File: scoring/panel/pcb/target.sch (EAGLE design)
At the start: 13 parts, among them J1 AVRISP6_COMPACT, U1 ATTINY85-20SU

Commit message: target panel: Get BOM into shape, and make an openoffice version with total and mechanical parts.
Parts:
- C1: PRICE10 (none) -> 0.05
- HIT: PRICE10 (none) -> 0.288
- J1: DPN (none) -> OR1108-ND; PRICE10 (none) -> 0.399
- JP1: DPN (none) -> 952-2245-ND; PRICE10 (none) -> 0.155
- JP2: DPN (none) -> 102-1170-ND; PRICE10 (none) -> 1.833
- PWR: PRICE10 (none) -> 0.267
- R1, R2, R3, R4: PRICE10 (none) -> 0.0196
- R6: DPN (none) -> P100ACT-ND; PRICE10 (none) -> 0.0196
- U1: PRICE10 (none) -> 1.386
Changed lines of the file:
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@@
 <part name="U1" library="Atmel_By_element14_Batch_1-00" deviceset="ATTINY85-20SU" device="">
 <attribute name="DPN" value="ATTINY85-20SU-ND"/>
+<attribute name="PRICE10" value="1.386"/>
 </part>
 <part name="P+1" library="supply1" deviceset="VCC" device=""/>
@@
 <part name="C1" library="rcl" deviceset="C-US" device="C0805" value=".1uF">
 <attribute name="DPN" value="399-1168-1-ND"/>
+<attribute name="PRICE10" value="0.05"/>
 </part>
 <part name="PWR" library="led" deviceset="LED" device="SML0805">
 <attribute name="DPN" value="160-1469-1-ND"/>
+<attribute name="PRICE10" value="0.267"/>
 </part>
 <part name="HIT" library="led" deviceset="LED" device="SML0805">
 <attribute name="DPN" value="160-1414-1-ND"/>
+<attribute name="PRICE10" value="0.288"/>
 </part>
 <part name="R1" library="rcl" deviceset="R-US_" device="R0805" value="680">
 <attribute name="DPN" value="P680ACT-ND"/>
+<attribute name="PRICE10" value="0.0196"/>
 </part>
 <part name="R2" library="rcl" deviceset="R-US_" device="R0805" value="680">
 <attribute name="DPN" value="P680ACT-ND"/>
+<attribute name="PRICE10" value="0.0196"/>
 </part>
 <part name="R3" library="rcl" deviceset="R-US_" device="R0805" value="10k">
 <attribute name="DPN" value="P10KACT-ND"/>
+<attribute name="PRICE10" value="0.0196"/>
 </part>
 <part name="R4" library="rcl" deviceset="R-US_" device="R0805" value="10k">
 <attribute name="DPN" value="P10KACT-ND"/>
+<attribute name="PRICE10" value="0.0196"/>
 </part>
 <part name="GND2" library="supply1" deviceset="GND" device=""/>
 <part name="P+2" library="supply1" deviceset="VCC" device=""/>
 <part name="P+3" library="supply1" deviceset="VCC" device=""/>
-<part name="J1" library="target" deviceset="AVRISP6" device="_COMPACT" value="AVRISP6_COMPACT"/>
+<part name="J1" library="target" deviceset="AVRISP6" device="_COMPACT" value="AVRISP6_COMPACT">
+<attribute name="DPN" value="OR1108-ND"/>
+<attribute name="PRICE10" value="0.399"/>
+</part>
 <part name="P+4" library="supply1" deviceset="VCC" device=""/>
 <part name="GND3" library="supply1" deviceset="GND" device=""/>
-<part name="JP1" library="pinhead" deviceset="PINHD-1X3" device=""/>
+<part name="JP1" library="pinhead" deviceset="PINHD-1X3" device="">
+<attribute name="DPN" value="952-2245-ND"/>
+<attribute name="PRICE10" value="0.155"/>
+</part>
 <part name="GND4" library="supply1" deviceset="GND" device=""/>
 <part name="P+5" library="supply1" deviceset="VCC" device=""/>
-<part name="JP2" library="pinhead" deviceset="PINHD-1X2" device=""/>
+<part name="JP2" library="pinhead" deviceset="PINHD-1X2" device="">
+<attribute name="DPN" value="102-1170-ND"/>
+<attribute name="PRICE10" value="1.833"/>
+</part>
 <part name="R5" library="rcl" deviceset="R-US_" device="R0805" value="DNP"/>
 <part name="R6" library="rcl" deviceset="R-US_" device="R0805" value="100">
-<attribute name="P100ACT-ND" value=""/>
+<attribute name="DPN" value="P100ACT-ND"/>
+<attribute name="PRICE10" value="0.0196"/>
 </part>
 </parts>
@@
 <instance part="U1" gate="A" x="33.02" y="43.18">
 <attribute name="DPN" x="33.02" y="43.18" size="1.778" layer="96" display="off"/>
+<attribute name="PRICE10" x="33.02" y="43.18" size="1.778" layer="96" display="off"/>
 </instance>
 <instance part="P+1" gate="VCC" x="10.16" y="53.34"/>
@@
 <instance part="C1" gate="G$1" x="-2.54" y="40.64">
 <attribute name="DPN" x="-2.54" y="40.64" size="1.778" layer="96" display="off"/>
+<attribute name="PRICE10" x="-2.54" y="40.64" size="1.778" layer="96" display="off"/>
 </instance>
 <instance part="PWR" gate="G$1" x="-22.86" y="27.94">
 <attribute name="DPN" x="-22.86" y="27.94" size="1.778" layer="96" display="off"/>
+<attribute name="PRICE10" x="-22.86" y="27.94" size="1.778" layer="96" display="off"/>
 </instance>
 <instance part="HIT" gate="G$1" x="88.9" y="50.8">
 <attribute name="DPN" x="88.9" y="50.8" size="1.778" layer="96" display="off"/>
+<attribute name="PRICE10" x="88.9" y="50.8" size="1.778" layer="96" display="off"/>
 </instance>
 <instance part="R1" gate="G$1" x="-22.86" y="40.64" rot="R90">
 <attribute name="DPN" x="-22.86" y="40.64" size="1.778" layer="96" rot="R90" display="off"/>
+<attribute name="PRICE10" x="-22.86" y="40.64" size="1.778" layer="96" rot="R90" display="off"/>
 </instance>
 <instance part="R2" gate="G$1" x="88.9" y="60.96" rot="R90">
 <attribute name="DPN" x="88.9" y="60.96" size="1.778" layer="96" rot="R90" display="off"/>
+<attribute name="PRICE10" x="88.9" y="60.96" size="1.778" layer="96" rot="R90" display="off"/>
 </instance>
 <instance part="R3" gate="G$1" x="76.2" y="30.48" rot="R90">
 <attribute name="DPN" x="76.2" y="30.48" size="1.778" layer="96" rot="R90" display="off"/>
+<attribute name="PRICE10" x="76.2" y="30.48" size="1.778" layer="96" rot="R90" display="off"/>
 </instance>
 <instance part="R4" gate="G$1" x="83.82" y="30.48" rot="R90">
 <attribute name="DPN" x="83.82" y="30.48" size="1.778" layer="96" rot="R90" display="off"/>
+<attribute name="PRICE10" x="83.82" y="30.48" size="1.778" layer="96" rot="R90" display="off"/>
 </instance>
 <instance part="GND2" gate="1" x="76.2" y="20.32"/>
 <instance part="P+2" gate="VCC" x="96.52" y="25.4"/>
 <instance part="P+3" gate="VCC" x="88.9" y="71.12"/>
-<instance part="J1" gate="A" x="33.02" y="71.12"/>
+<instance part="J1" gate="A" x="33.02" y="71.12">
+<attribute name="DPN" x="33.02" y="71.12" size="1.778" layer="96" display="off"/>
+<attribute name="PRICE10" x="33.02" y="71.12" size="1.778" layer="96" display="off"/>
+</instance>
 <instance part="P+4" gate="VCC" x="12.7" y="86.36"/>
 <instance part="GND3" gate="1" x="12.7" y="71.12"/>
-<instance part="JP1" gate="A" x="114.3" y="53.34"/>
+<instance part="JP1" gate="A" x="114.3" y="53.34">
+<attribute name="DPN" x="114.3" y="53.34" size="1.778" layer="96" display="off"/>
+<attribute name="PRICE10" x="114.3" y="53.34" size="1.778" layer="96" display="off"/>
+</instance>
 <instance part="GND4" gate="1" x="104.14" y="45.72"/>
 <instance part="P+5" gate="VCC" x="104.14" y="63.5"/>
-<instance part="JP2" gate="G$1" x="121.92" y="35.56"/>
+<instance part="JP2" gate="G$1" x="121.92" y="35.56">
+<attribute name="DPN" x="121.92" y="35.56" size="1.778" layer="96" display="off"/>
+<attribute name="PRICE10" x="121.92" y="35.56" size="1.778" layer="96" display="off"/>
+</instance>
 <instance part="R5" gate="G$1" x="106.68" y="35.56" rot="R90"/>
 <instance part="R6" gate="G$1" x="99.06" y="35.56" rot="R90">
-<attribute name="P100ACT-ND" x="99.06" y="35.56" size="1.778" layer="96" rot="R90" display="off"/>
+<attribute name="DPN" x="99.06" y="35.56" size="1.778" layer="96" rot="R90" display="off"/>
+<attribute name="PRICE10" x="99.06" y="35.56" size="1.778" layer="96" rot="R90" display="off"/>
 </instance>
 </instances>

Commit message: Panel PCB: Update the decoupling cap to be a 1uF one instead of 0.1uF.
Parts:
- C1: value .1uF -> 1uF; DPN 399-1168-1-ND -> 399-8004-1-ND; PRICE10 0.05 -> 0.13
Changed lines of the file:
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@@
 <part name="P+1" library="supply1" deviceset="VCC" device=""/>
 <part name="GND1" library="supply1" deviceset="GND" device=""/>
-<part name="C1" library="rcl" deviceset="C-US" device="C0805" value=".1uF">
-<attribute name="DPN" value="399-1168-1-ND"/>
-<attribute name="PRICE10" value="0.05"/>
+<part name="C1" library="rcl" deviceset="C-US" device="C0805" value="1uF">
+<attribute name="DPN" value="399-8004-1-ND"/>
+<attribute name="PRICE10" value="0.13"/>
 </part>
 <part name="PWR" library="led" deviceset="LED" device="SML0805">

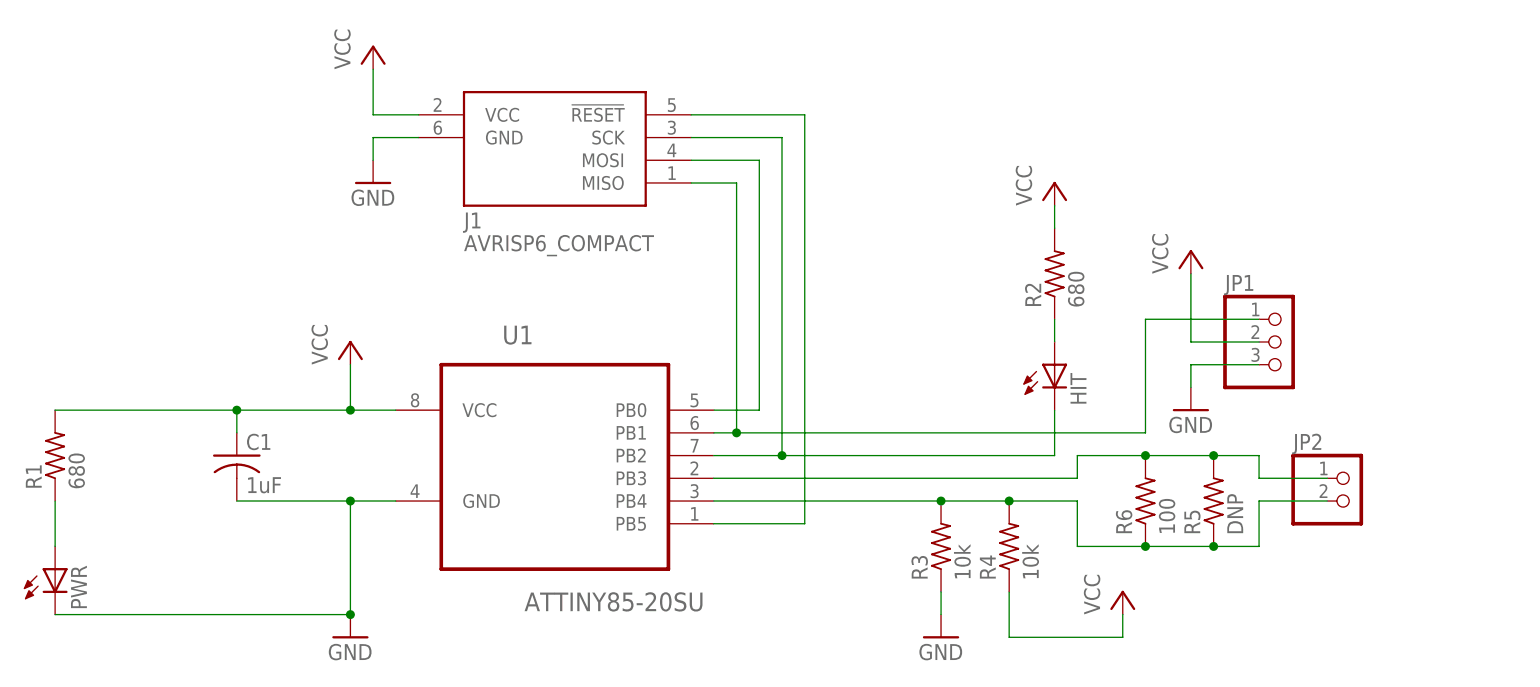
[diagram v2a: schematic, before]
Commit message: Draft of scoring panel with mounting holes slightly closer to the edge, converted to use macrofab parts, with a JST connector, and a pullup on the signal line.
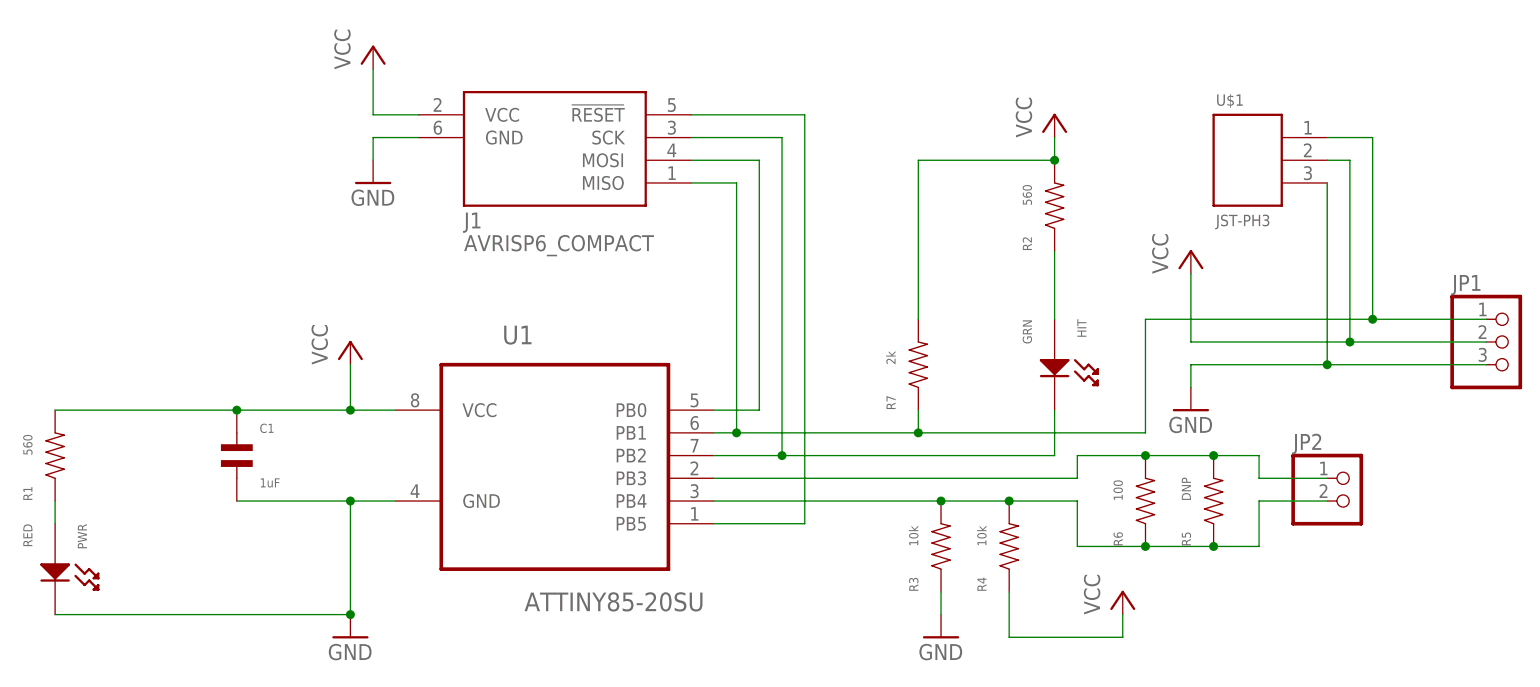
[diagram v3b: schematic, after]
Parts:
- added R7: 2k, MF_Passives:RESISTOR_0603
- added U$1: JST-PH3, jst-ph:JST-PH3
- C1: device rcl:C-USC0805 -> MF_Passives:CAPACITOR_NP_0603; DPN 399-8004-1-ND -> (none); PRICE10 0.13 -> (none)
- HIT: value (none) -> GRN; device led:LEDSML0805 -> MF_LEDs:LED_SINGLE_0603; DPN 160-1414-1-ND -> (none); PRICE10 0.288 -> (none)
- PWR: value (none) -> RED; device led:LEDSML0805 -> MF_LEDs:LED_SINGLE_0603; DPN 160-1469-1-ND -> (none); PRICE10 0.267 -> (none)
- R1, R2: value 680 -> 560; device rcl:R-US_R0805 -> MF_Passives:RESISTOR_0603
- R3, R4, R5, R6: device rcl:R-US_R0805 -> MF_Passives:RESISTOR_0603
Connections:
- net GND: now also C1.P$2, PWR.CATHODE, R3.P$1, U$1.3; no longer C1.2, PWR.C, R3.1
- net N$1: now also PWR.ANODE, R1.P$1; no longer PWR.A, R1.1
- net N$3: now also R3.P$2, R4.P$2, R5.P$1, R6.P$1; no longer R3.2, R4.2, R5.1, R6.1
- net N$4: now also HIT.CATHODE; no longer HIT.C
- net N$5: now also R2.P$1; no longer HIT.A, R2.1
- net N$6: now also R5.P$2, R6.P$2; no longer R5.2, R6.2
- net N$8: now also R7.P$1, U$1.1
- net VCC: now also C1.P$1, R1.P$2, R2.P$2, R4.P$1, R7.P$2, U$1.2; no longer C1.1, R1.2, R2.2, R4.1
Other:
- moved on the sheet: C1, JP1, R2

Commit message: Add resistor inline on signal line.  Run ERC and DRC.
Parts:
- added R8: 47, MF_Passives:RESISTOR_0603
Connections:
- new net N$9: J1.MISO, R8.P$1, U1.PB1
- net N$5: now also HIT.ANODE
- net N$8: now also R8.P$2; no longer J1.MISO, U1.PB1
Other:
- moved on the sheet: R7
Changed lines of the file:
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@@
 <part name="R7" library="MF_Passives" deviceset="RESISTOR" device="_0603" value="2k"/>
 <part name="U$1" library="jst-ph" deviceset="JST-PH3" device=""/>
+<part name="R8" library="MF_Passives" deviceset="RESISTOR" device="_0603" value="47"/>
 </parts>
 <sheets>
@@
 <instance part="HIT" gate="G$1" x="88.9" y="50.8" rot="R270"/>
 <instance part="C1" gate="G$1" x="-2.54" y="40.64"/>
-<instance part="R7" gate="G$1" x="73.66" y="50.8" rot="R90"/>
+<instance part="R7" gate="G$1" x="78.74" y="50.8" rot="R90"/>
 <instance part="U$1" gate="A" x="109.22" y="73.66"/>
+<instance part="R8" gate="G$1" x="68.58" y="43.18"/>
 </instances>
 <busses>
@@
 <wire x1="88.9" y1="76.2" x2="88.9" y2="73.66" width="0.1524" layer="91"/>
 <pinref part="R7" gate="G$1" pin="P$2"/>
-<wire x1="73.66" y1="55.88" x2="73.66" y2="73.66" width="0.1524" layer="91"/>
-<wire x1="73.66" y1="73.66" x2="88.9" y2="73.66" width="0.1524" layer="91"/>
+<wire x1="78.74" y1="55.88" x2="78.74" y2="73.66" width="0.1524" layer="91"/>
+<wire x1="78.74" y1="73.66" x2="88.9" y2="73.66" width="0.1524" layer="91"/>
 <junction x="88.9" y="73.66"/>
 </segment>
@@
 </segment>
 </net>
-<net name="N$5" class="0">
-<segment>
-<pinref part="R2" gate="G$1" pin="P$1"/>
-<wire x1="88.9" y1="63.5" x2="88.9" y2="55.88" width="0.1524" layer="91"/>
-</segment>
-</net>
 <net name="N$2" class="0">
 <segment>
@@
 <net name="N$8" class="0">
 <segment>
-<pinref part="J1" gate="A" pin="MISO"/>
-<wire x1="48.26" y1="71.12" x2="53.34" y2="71.12" width="0.1524" layer="91"/>
-<wire x1="53.34" y1="71.12" x2="53.34" y2="43.18" width="0.1524" layer="91"/>
-<pinref part="U1" gate="A" pin="PB1"/>
-<wire x1="53.34" y1="43.18" x2="50.8" y2="43.18" width="0.1524" layer="91"/>
-<wire x1="53.34" y1="43.18" x2="73.66" y2="43.18" width="0.1524" layer="91"/>
-<wire x1="73.66" y1="43.18" x2="99.06" y2="43.18" width="0.1524" layer="91"/>
+<wire x1="78.74" y1="43.18" x2="99.06" y2="43.18" width="0.1524" layer="91"/>
 <wire x1="99.06" y1="43.18" x2="99.06" y2="55.88" width="0.1524" layer="91"/>
-<junction x="53.34" y="43.18"/>
 <pinref part="JP1" gate="A" pin="1"/>
 <wire x1="99.06" y1="55.88" x2="124.46" y2="55.88" width="0.1524" layer="91"/>
 <pinref part="R7" gate="G$1" pin="P$1"/>
 <wire x1="124.46" y1="55.88" x2="137.16" y2="55.88" width="0.1524" layer="91"/>
-<wire x1="73.66" y1="45.72" x2="73.66" y2="43.18" width="0.1524" layer="91"/>
-<junction x="73.66" y="43.18"/>
+<wire x1="78.74" y1="45.72" x2="78.74" y2="43.18" width="0.1524" layer="91"/>
 <pinref part="U$1" gate="A" pin="1"/>
 <wire x1="119.38" y1="76.2" x2="124.46" y2="76.2" width="0.1524" layer="91"/>
 <wire x1="124.46" y1="76.2" x2="124.46" y2="55.88" width="0.1524" layer="91"/>
 <junction x="124.46" y="55.88"/>
+<pinref part="R8" gate="G$1" pin="P$2"/>
+<wire x1="73.66" y1="43.18" x2="78.74" y2="43.18" width="0.1524" layer="91"/>
+<junction x="78.74" y="43.18"/>
 </segment>
 </net>
@@
 </segment>
 </net>
+<net name="N$9" class="0">
+<segment>
+<pinref part="U1" gate="A" pin="PB1"/>
+<pinref part="J1" gate="A" pin="MISO"/>
+<wire x1="48.26" y1="71.12" x2="53.34" y2="71.12" width="0.1524" layer="91"/>
+<wire x1="53.34" y1="71.12" x2="53.34" y2="43.18" width="0.1524" layer="91"/>
+<wire x1="53.34" y1="43.18" x2="50.8" y2="43.18" width="0.1524" layer="91"/>
+<pinref part="R8" gate="G$1" pin="P$1"/>
+<wire x1="53.34" y1="43.18" x2="63.5" y2="43.18" width="0.1524" layer="91"/>
+<junction x="53.34" y="43.18"/>
+</segment>
+</net>
+<net name="N$5" class="0">
+<segment>
+<pinref part="HIT" gate="G$1" pin="ANODE"/>
+<pinref part="R2" gate="G$1" pin="P$1"/>
+<wire x1="88.9" y1="55.88" x2="88.9" y2="63.5" width="0.1524" layer="91"/>
+</segment>
+</net>
 </nets>
 </sheet>
 </sheets>
+<errors>
+</errors>
 </schematic>
 </drawing>
